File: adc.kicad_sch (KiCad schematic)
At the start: 34 parts, among them U7 AD7177-2BRUZ, U70 TG2520SMN-16M-MCG, U75 OPA2189DGK

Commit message: Front panel
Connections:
- net SYNC: now reaches U7.15 (~{SYNC}/~{ERROR})
- no-connect marks 8 -> 7
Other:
- moved on the sheet: C775
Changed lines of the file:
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@@
-	)
-	(no_connect
-		(at 199.39 63.5)
 	)
 	(no_connect
@@
 	(wire
 		(pts
+			(xy 204.47 55.88) (xy 199.39 55.88)
+		)
+		(stroke
+			(width 0)
+			(type default)
+		)
+	)
+	(wire
+		(pts
 			(xy 101.6 96.52) (xy 116.84 96.52)
 		)
@@
 	(wire
 		(pts
+			(xy 199.39 63.5) (xy 203.2 63.5)
+		)
+		(stroke
+			(width 0)
+			(type default)
+		)
+	)
+	(wire
+		(pts
 			(xy 200.66 58.42) (xy 199.39 58.42)
 		)
@@
 	(wire
 		(pts
-			(xy 203.2 63.5) (xy 203.2 58.42)
+			(xy 203.2 60.96) (xy 203.2 58.42)
 		)
 		(stroke
@@
 	(wire
 		(pts
+			(xy 204.47 53.34) (xy 204.47 55.88)
+		)
+		(stroke
+			(width 0)
+			(type default)
+		)
+	)
+	(wire
+		(pts
 			(xy 175.26 105.41) (xy 172.72 105.41)
 		)
@@
 	(wire
 		(pts
-			(xy 199.39 55.88) (xy 207.01 55.88)
+			(xy 204.47 53.34) (xy 208.28 53.34)
 		)
 		(stroke
@@
 	(wire
 		(pts
-			(xy 203.2 63.5) (xy 207.01 63.5)
+			(xy 203.2 60.96) (xy 208.28 60.96)
 		)
 		(stroke
@@
 		(shape input)
 		(at 203.2 66.04 0)
+		(effects
+			(font
+				(size 1.27 1.27)
+			)
+			(justify left)
+		)
+	)
+	(hierarchical_label "SYNC"
+		(shape bidirectional)
+		(at 203.2 63.5 0)
 		(effects
 			(font
@@
 	(symbol
 		(lib_id "Device:C")
-		(at 207.01 59.69 0)
+		(at 208.28 57.15 0)
 		(unit 1)
 		(exclude_from_sim no)
@@
 		(dnp no)
 		(property "Reference" "C775"
-			(at 207.01 61.7219 0)
+			(at 208.28 59.1819 0)
 			(effects
 				(font
@@
 		)
 		(property "Value" "1u"
-			(at 207.01 57.6579 0)
+			(at 208.28 55.1179 0)
 			(effects
 				(font
@@
 		)
 		(property "Footprint" "Capacitor_SMD:C_0402_1005Metric"
-			(at 207.9752 63.5 0)
+			(at 209.2452 60.96 0)
 			(effects
 				(font
@@
 		)
 		(property "Datasheet" "25V"
-			(at 207.01 59.69 0)
+			(at 208.28 57.15 0)
 			(effects
 				(font
@@
 		)
 		(property "Description" "Unpolarized capacitor"
-			(at 207.01 59.69 0)
+			(at 208.28 57.15 0)
 			(effects
 				(font
@@
 		)
 		(property "LCSC" "C52923"
-			(at 207.01 59.69 0)
+			(at 208.28 57.15 0)
 			(effects
 				(font
@@
 		)
 		(property "Stock" "JLC"
-			(at 207.01 59.69 0)
-			(effects
-				(font
+			(at 208.28 57.15 0)
+			(effects
+				(font

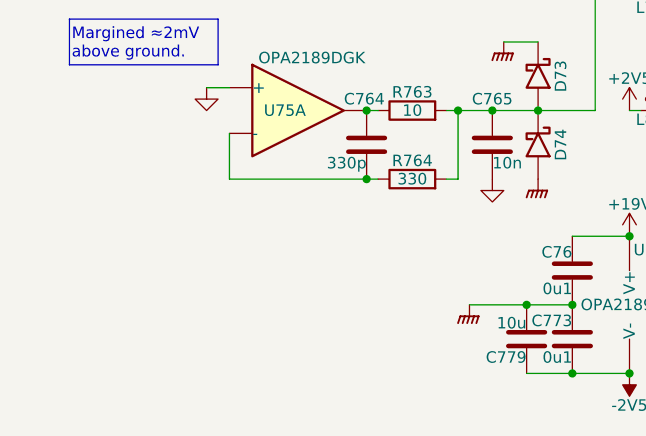
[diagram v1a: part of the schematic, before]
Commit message: Change some footprints.
Mounting holes for covers.
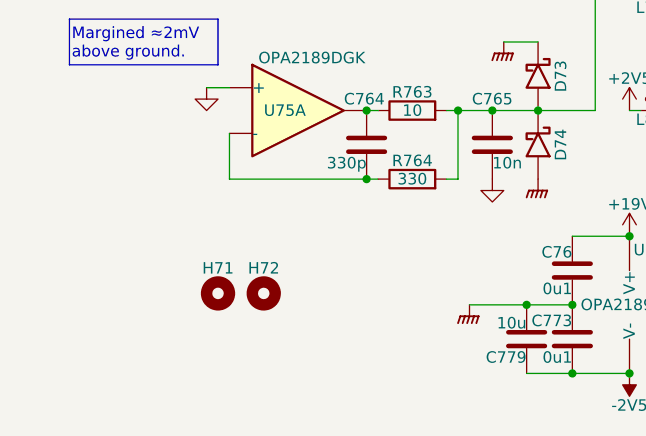
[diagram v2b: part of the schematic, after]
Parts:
- added H71, H72: MountingHole, Parts:Hole_1.5mm_Unplated, symbol Mechanical:MountingHole
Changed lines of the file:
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@@
+	)
+	(symbol
+		(lib_id "Mechanical:MountingHole")
+		(at 105.41 109.22 0)
+		(unit 1)
+		(exclude_from_sim no)
+		(in_bom no)
+		(on_board yes)
+		(dnp no)
+		(property "Reference" "H72"
+			(at 105.41 106.426 0)
+			(effects
+				(font
+					(size 1.27 1.27)
+				)
+			)
+		)
+		(property "Value" "MountingHole"
+			(at 105.41 106.045 0)
+			(effects
+				(font
+					(size 1.27 1.27)
+				)
+				(hide yes)
+			)
+		)
+		(property "Footprint" "Parts:Hole_1.5mm_Unplated"
+			(at 105.41 109.22 0)
+			(effects
+				(font
+					(size 1.27 1.27)
+				)
+				(hide yes)
+			)
+		)
+		(property "Datasheet" "~"
+			(at 105.41 109.22 0)
+			(effects
+				(font
+					(size 1.27 1.27)
+				)
+				(hide yes)
+			)
+		)
+		(property "Description" "Mounting Hole without connection"
+			(at 105.41 109.22 0)
+			(effects
+				(font
+					(size 1.27 1.27)
+				)
+				(hide yes)
+			)
+		)
+		(instances
+			(project "lincal"
+				(path "/b054cef4-39e3-49d8-aff0-7ba5a206c187/e69ade03-efa5-476d-a99a-7096b679a0cf"
+					(reference "H72")
+					(unit 1)
+				)
+			)
+		)
 	)
 	(symbol
@@
 					(unit 1)
 				)
+			)
+		)
+	)
+	(symbol
+		(lib_id "Mechanical:MountingHole")
+		(at 100.33 109.22 0)
+		(unit 1)
+		(exclude_from_sim no)
+		(in_bom no)
+		(on_board yes)
+		(dnp no)
+		(property "Reference" "H71"
+			(at 100.33 106.426 0)
+			(effects
+				(font
+					(size 1.27 1.27)
+				)
+			)
+		)
+		(property "Value" "MountingHole"
+			(at 100.33 106.045 0)
+			(effects
+				(font
+					(size 1.27 1.27)
+				)
+				(hide yes)
+			)
+		)
+		(property "Footprint" "Parts:Hole_1.5mm_Unplated"
+			(at 100.33 109.22 0)
+			(effects
+				(font
+					(size 1.27 1.27)
+				)
+				(hide yes)
+			)
+		)
+		(property "Datasheet" "~"
+			(at 100.33 109.22 0)
+			(effects
+				(font
+					(size 1.27 1.27)
+				)
+				(hide yes)
+			)
+		)
+		(property "Description" "Mounting Hole without connection"
+			(at 100.33 109.22 0)
+			(effects
+				(font
+					(size 1.27 1.27)
+				)
+				(hide yes)
+			)
+		)
+		(instances
+			(project "lincal"
+				(path "/b054cef4-39e3-49d8-aff0-7ba5a206c187/e69ade03-efa5-476d-a99a-7096b679a0cf"
+					(reference "H71")
+					(unit 1)
+				)

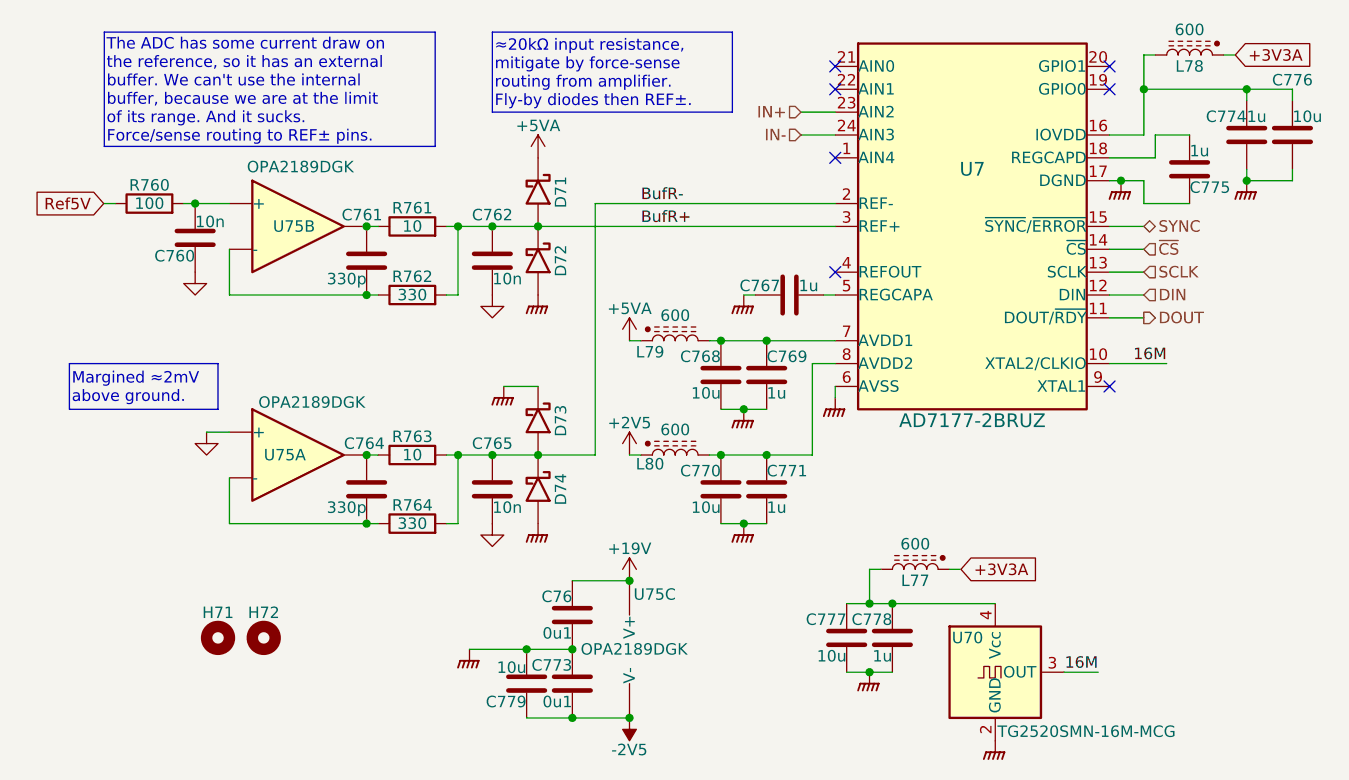
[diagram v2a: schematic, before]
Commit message: Simplify relay drive.
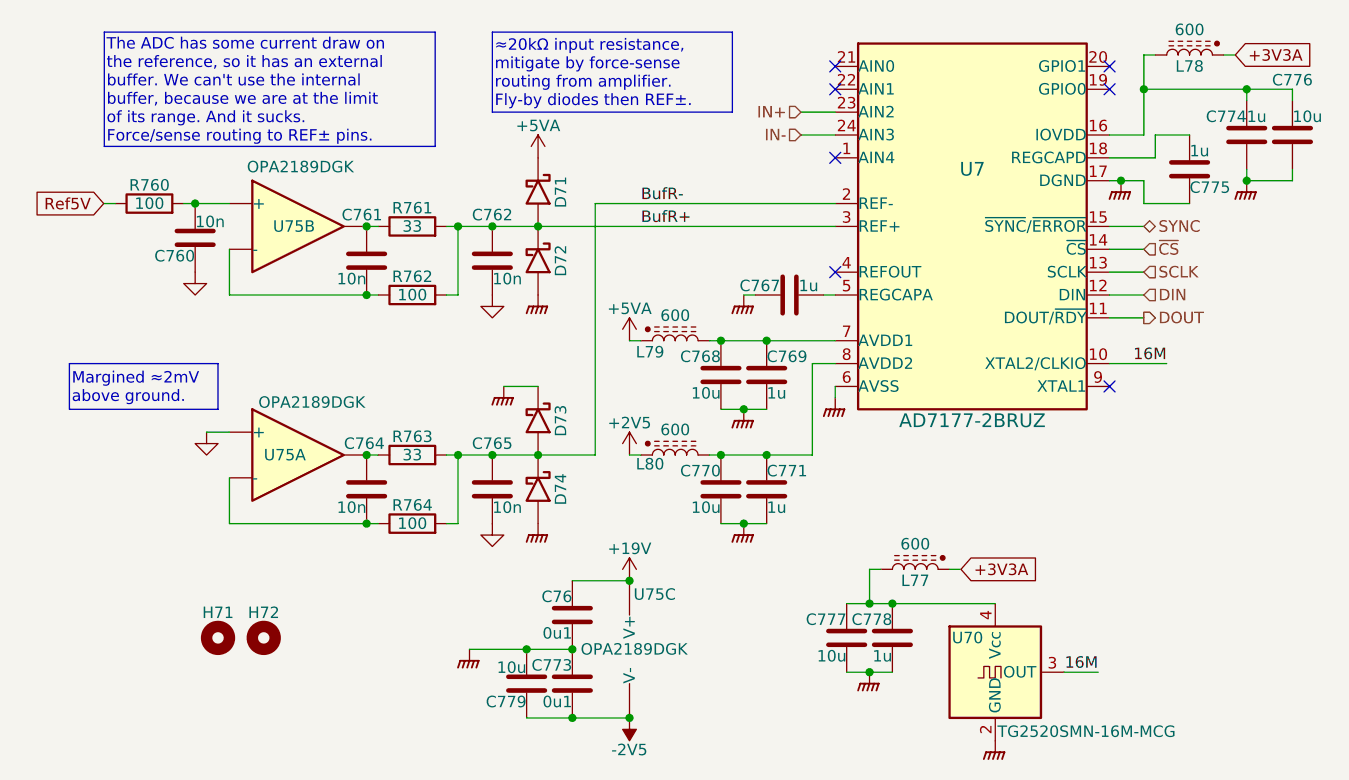
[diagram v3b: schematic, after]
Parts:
- C761, C764: value 330p -> 10n; LCSC C1664 -> C307500
- R761, R763: value 10 -> 33; LCSC C25077 -> C25105
- R762, R764: value 330 -> 100; LCSC C25104 -> C25076
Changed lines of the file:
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@@
 			)
 		)
-		(property "Value" "10"
+		(property "Value" "33"
 			(at 121.92 88.9 90)
 			(effects
@@
 			)
 		)
-		(property "LCSC" "C25077"
+		(property "LCSC" "C25105"
 			(at 121.92 88.9 90)
 			(effects
@@
 			)
 		)
-		(property "Value" "330"
+		(property "Value" "100"
 			(at 121.92 71.12 90)
 			(effects
@@
 			)
 		)
-		(property "LCSC" "C25104"
+		(property "LCSC" "C25076"
 			(at 121.92 71.12 90)
 			(effects
@@
 			)
 		)
-		(property "Value" "330"
+		(property "Value" "100"
 			(at 121.92 96.52 90)
 			(effects
@@
 			)
 		)
-		(property "LCSC" "C25104"
+		(property "LCSC" "C25076"
 			(at 121.92 96.52 90)
 			(effects
@@
 			)
 		)
-		(property "Value" "330p"
+		(property "Value" "10n"
 			(at 116.84 69.342 0)
 			(effects
@@
 			)
 		)
-		(property "Datasheet" "C0G, 50V"
+		(property "Datasheet" "C0G, 25V"
 			(at 116.84 67.31 0)
 			(effects
@@
 			)
 		)
-		(property "LCSC" "C1664"
+		(property "LCSC" "C307500"
 			(at 116.84 67.31 0)
 			(effects
@@
 			)
 		)
-		(property "Value" "10"
+		(property "Value" "33"
 			(at 121.92 63.5 90)
 			(effects
@@
 			)
 		)
-		(property "LCSC" "C25077"
+		(property "LCSC" "C25105"
 			(at 121.92 63.5 90)
 			(effects
@@
 			)
 		)
-		(property "Value" "330p"
+		(property "Value" "10n"
 			(at 116.84 94.742 0)
 			(effects
@@
 			)
 		)
-		(property "Datasheet" "C0G, 50V"
+		(property "Datasheet" "C0G, 25V"
 			(at 116.84 92.71 0)
 			(effects
@@
 			)
 		)
-		(property "LCSC" "C1664"
+		(property "LCSC" "C307500"
 			(at 116.84 92.71 0)
 			(effects

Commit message: Tweak various feedback loops.
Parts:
- H71, H72: Stock (none) -> Board
- U70: Stock ? -> Digikey
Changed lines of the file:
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@@
+			)
+		)
+		(property "Stock" "Board"
+			(at 105.41 109.22 0)
+			(effects
+				(font
+					(size 1.27 1.27)
+				)
+				(hide yes)
 			)
 		)
@@
 		)
 		(property "Description" "Mounting Hole without connection"
+			(at 100.33 109.22 0)
+			(effects
+				(font
+					(size 1.27 1.27)
+				)
+				(hide yes)
+			)
+		)
+		(property "Stock" "Board"
 			(at 100.33 109.22 0)
 			(effects
@@
 			)
 		)
-		(property "Stock" "?"
+		(property "Stock" "Digikey"
 			(at 186.69 113.03 0)
 			(effects

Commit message: Readyish
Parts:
- C760, C761, C762, C764, C765: LCSC C307500 -> C389113
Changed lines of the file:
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@@
 			)
 		)
-		(property "Datasheet" "C0G, 25V"
+		(property "Datasheet" "C0G, 50V"
 			(at 130.81 67.31 0)
 			(effects
@@
 			)
 		)
-		(property "LCSC" "C307500"
+		(property "LCSC" "C389113"
 			(at 130.81 67.31 0)
 			(effects
@@
 			)
 		)
-		(property "Datasheet" "C0G, 25V"
+		(property "Datasheet" "C0G, 50V"
 			(at 130.81 92.71 0)
 			(effects
@@
 			)
 		)
-		(property "LCSC" "C307500"
+		(property "LCSC" "C389113"
 			(at 130.81 92.71 0)
 			(effects
@@
 			)
 		)
-		(property "Datasheet" "C0G, 25V"
+		(property "Datasheet" "C0G, 50V"
 			(at 116.84 67.31 0)
 			(effects
@@
 			)
 		)
-		(property "LCSC" "C307500"
+		(property "LCSC" "C389113"
 			(at 116.84 67.31 0)
 			(effects
@@
 			)
 		)
-		(property "Datasheet" "C0G, 25V"
+		(property "Datasheet" "C0G, 50V"
 			(at 97.79 64.77 0)
 			(effects
@@
 			)
 		)
-		(property "LCSC" "C307500"
+		(property "LCSC" "C389113"
 			(at 97.79 64.77 0)
 			(effects
@@
 			)
 		)
-		(property "Datasheet" "C0G, 25V"
+		(property "Datasheet" "C0G, 50V"
 			(at 116.84 92.71 0)
 			(effects
@@
 			)
 		)
-		(property "LCSC" "C307500"
+		(property "LCSC" "C389113"
 			(at 116.84 92.71 0)
 			(effects
